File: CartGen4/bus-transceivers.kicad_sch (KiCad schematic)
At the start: 5 parts, among them U4 NXS0108BQX, U6 NXS0108BQX, U7 NXS0108BQX, U8 NXS0104BQX

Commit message: Made general component placement + fixed ADDR
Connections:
- net GB_5V_A0: now also U7.12 (B8); no longer U7.20 (B1)
- net GB_5V_A1: now also U7.13 (B7); no longer U7.18 (B2)
- net GB_5V_A10: now also U6.14 (B6); no longer U6.17 (B3)
- net GB_5V_A11: now also U6.15 (B5); no longer U6.16 (B4)
- net GB_5V_A12: now also U6.16 (B4); no longer U6.15 (B5)
- net GB_5V_A13: now also U6.17 (B3); no longer U6.14 (B6)
- net GB_5V_A14: now also U6.18 (B2); no longer U6.13 (B7)
- net GB_5V_A15: now also U6.20 (B1); no longer U6.12 (B8)
- net GB_5V_A2: now also U7.14 (B6); no longer U7.17 (B3)
- net GB_5V_A3: now also U7.15 (B5); no longer U7.16 (B4)
- net GB_5V_A4: now also U7.16 (B4); no longer U7.15 (B5)
- net GB_5V_A5: now also U7.17 (B3); no longer U7.14 (B6)
- net GB_5V_A6: now also U7.18 (B2); no longer U7.13 (B7)
- net GB_5V_A7: now also U7.20 (B1); no longer U7.12 (B8)
- net GB_5V_A8: now also U6.12 (B8); no longer U6.20 (B1)
- net GB_5V_A9: now also U6.13 (B7); no longer U6.18 (B2)
- net GB_A0: now also U7.9 (A8); no longer U7.1 (A1)
- net GB_A1: now also U7.8 (A7); no longer U7.3 (A2)
- net GB_A10: now also U6.7 (A6); no longer U6.4 (A3)
- net GB_A11: now also U6.6 (A5); no longer U6.5 (A4)
- net GB_A12: now also U6.5 (A4); no longer U6.6 (A5)
- net GB_A13: now also U6.4 (A3); no longer U6.7 (A6)
- net GB_A14: now also U6.3 (A2); no longer U6.8 (A7)
- net GB_A15: now also U6.1 (A1); no longer U6.9 (A8)
- net GB_A2: now also U7.7 (A6); no longer U7.4 (A3)
- net GB_A3: now also U7.6 (A5); no longer U7.5 (A4)
- net GB_A4: now also U7.5 (A4); no longer U7.6 (A5)
- net GB_A5: now also U7.4 (A3); no longer U7.7 (A6)
- net GB_A6: now also U7.3 (A2); no longer U7.8 (A7)
- net GB_A7: now also U7.1 (A1); no longer U7.9 (A8)
- net GB_A8: now also U6.9 (A8); no longer U6.1 (A1)
- net GB_A9: now also U6.8 (A7); no longer U6.3 (A2)
- net GB_CLK: now also U8.5 (A4); no longer U8.2 (A1)
- net GB_CLK_5V: now also U8.10 (B4); no longer U8.13 (B1)
- net GB_CS#: now also U8.2 (A1); no longer U8.4 (A3)
- net GB_CS#_5V: now also U8.13 (B1); no longer U8.11 (B3)
- net GB_RD#: now also U8.3 (A2); no longer U8.5 (A4)
- net GB_RD#_5V: now also U8.12 (B2); no longer U8.10 (B4)
- net GB_WR#: now also U8.4 (A3); no longer U8.3 (A2)
- net GB_WR#_5V: now also U8.11 (B3); no longer U8.12 (B2)

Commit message: Changed most R and C to 0402 size
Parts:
- R14: footprint Resistor_SMD:R_0603_1608Metric_Pad0.98x0.95mm_HandSolder -> Resistor_SMD:R_0402_1005Metric_Pad0.72x0.64mm_HandSolder
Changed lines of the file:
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@@
       (effects (font (size 1.27 1.27)) (justify left))
     )
-    (property "Footprint" "Resistor_SMD:R_0603_1608Metric_Pad0.98x0.95mm_HandSolder" (id 2) (at 47.752 73.66 90)
+    (property "Footprint" "Resistor_SMD:R_0402_1005Metric_Pad0.72x0.64mm_HandSolder" (id 2) (at 47.752 73.66 90)
       (effects (font (size 1.27 1.27)) hide)
     )

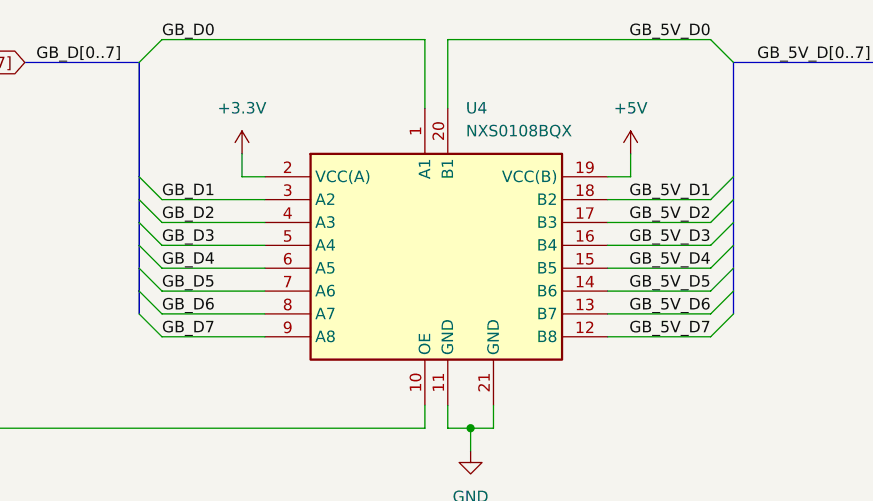
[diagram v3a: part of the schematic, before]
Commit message: Wired power supply
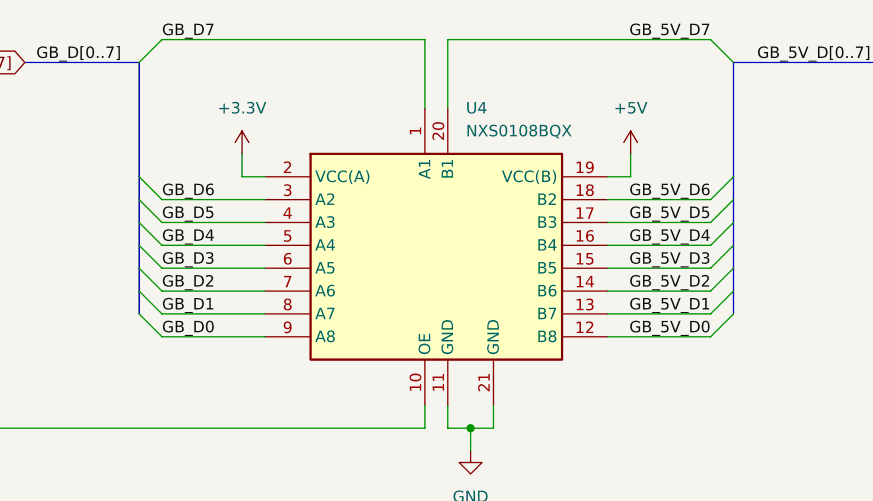
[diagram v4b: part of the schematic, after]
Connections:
- net GB_5V_D0: now also U4.12 (B8); no longer U4.20 (B1)
- net GB_5V_D1: now also U4.13 (B7); no longer U4.18 (B2)
- net GB_5V_D2: now also U4.14 (B6); no longer U4.17 (B3)
- net GB_5V_D3: now also U4.15 (B5); no longer U4.16 (B4)
- net GB_5V_D4: now also U4.16 (B4); no longer U4.15 (B5)
- net GB_5V_D5: now also U4.17 (B3); no longer U4.14 (B6)
- net GB_5V_D6: now also U4.18 (B2); no longer U4.13 (B7)
- net GB_5V_D7: now also U4.20 (B1); no longer U4.12 (B8)
- net GB_D0: now also U4.9 (A8); no longer U4.1 (A1)
- net GB_D1: now also U4.8 (A7); no longer U4.3 (A2)
- net GB_D2: now also U4.7 (A6); no longer U4.4 (A3)
- net GB_D3: now also U4.6 (A5); no longer U4.5 (A4)
- net GB_D4: now also U4.5 (A4); no longer U4.6 (A5)
- net GB_D5: now also U4.4 (A3); no longer U4.7 (A6)
- net GB_D6: now also U4.3 (A2); no longer U4.8 (A7)
- net GB_D7: now also U4.1 (A1); no longer U4.9 (A8)
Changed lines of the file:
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@@
+    (effects (font (size 1.27 1.27)) (justify left bottom))
+  )
+  (label "GB_D4" (at 97.79 46.99 0)
     (effects (font (size 1.27 1.27)) (justify left bottom))
   )
@@
     (effects (font (size 1.27 1.27)) (justify left bottom))
   )
-  (label "GB_D0" (at 97.79 24.13 0)
-    (effects (font (size 1.27 1.27)) (justify left bottom))
+  (label "GB_5V_A[0..7]" (at 176.53 144.78 180)
+    (effects (font (size 1.27 1.27)) (justify right bottom))
   )
-  (label "GB_5V_A[0..7]" (at 176.53 144.78 180)
+  (label "GB_5V_D7" (at 158.75 24.13 180)
+    (effects (font (size 1.27 1.27)) (justify right bottom))
+  )
+  (label "GB_5V_D6" (at 158.75 41.91 180)
     (effects (font (size 1.27 1.27)) (justify right bottom))
   )
@@
     (effects (font (size 1.27 1.27)) (justify right bottom))
   )
-  (label "GB_5V_D5" (at 158.75 52.07 180)
-    (effects (font (size 1.27 1.27)) (justify right bottom))
+  (label "GB_D0" (at 97.79 57.15 0)
+    (effects (font (size 1.27 1.27)) (justify left bottom))
   )
-  (label "GB_5V_D2" (at 158.75 44.45 180)
+  (label "GB_D1" (at 97.79 54.61 0)
+    (effects (font (size 1.27 1.27)) (justify left bottom))
+  )
+  (label "GB_5V_D0" (at 158.75 57.15 180)
     (effects (font (size 1.27 1.27)) (justify right bottom))
   )
@@
   (label "GB_5V_A14" (at 158.75 100.33 180)
     (effects (font (size 1.27 1.27)) (justify right bottom))
-  )
-  (label "GB_D1" (at 97.79 41.91 0)
-    (effects (font (size 1.27 1.27)) (justify left bottom))
   )
   (label "GB_A12" (at 97.79 105.41 0)
@@
     (effects (font (size 1.27 1.27)) (justify left bottom))
   )
-  (label "GB_D7" (at 97.79 57.15 0)
-    (effects (font (size 1.27 1.27)) (justify left bottom))
-  )
-  (label "GB_5V_D3" (at 158.75 46.99 180)
+  (label "GB_5V_D5" (at 158.75 44.45 180)
     (effects (font (size 1.27 1.27)) (justify right bottom))
   )
@@
     (effects (font (size 1.27 1.27)) (justify left bottom))
   )
+  (label "GB_5V_D2" (at 158.75 52.07 180)
+    (effects (font (size 1.27 1.27)) (justify right bottom))
+  )
   (label "GB_5V_A11" (at 158.75 107.95 180)
     (effects (font (size 1.27 1.27)) (justify right bottom))
   )
-  (label "GB_5V_D1" (at 158.75 41.91 180)
+  (label "GB_5V_D1" (at 158.75 54.61 180)
     (effects (font (size 1.27 1.27)) (justify right bottom))
   )
@@
     (effects (font (size 1.27 1.27)) (justify right bottom))
   )
-  (label "GB_D3" (at 97.79 46.99 0)
-    (effects (font (size 1.27 1.27)) (justify left bottom))
-  )
   (label "GB_A1" (at 97.79 172.72 0)
     (effects (font (size 1.27 1.27)) (justify left bottom))
-  )
-  (label "GB_5V_D0" (at 158.75 24.13 180)
-    (effects (font (size 1.27 1.27)) (justify right bottom))
   )
   (label "GB_5V_A10" (at 158.75 110.49 180)
     (effects (font (size 1.27 1.27)) (justify right bottom))
   )
-  (label "GB_5V_D7" (at 158.75 57.15 180)
+  (label "GB_5V_D3" (at 158.75 49.53 180)
     (effects (font (size 1.27 1.27)) (justify right bottom))
   )
@@
     (effects (font (size 1.27 1.27)) (justify left bottom))
   )
-  (label "GB_A3" (at 97.79 167.64 0)
+  (label "GB_5V_D4" (at 158.75 46.99 180)
+    (effects (font (size 1.27 1.27)) (justify right bottom))
+  )
+  (label "GB_D6" (at 97.79 41.91 0)
     (effects (font (size 1.27 1.27)) (justify left bottom))
   )
-  (label "GB_5V_D6" (at 158.75 54.61 180)
-    (effects (font (size 1.27 1.27)) (justify right bottom))
-  )
-  (label "GB_D5" (at 97.79 52.07 0)
+  (label "GB_A3" (at 97.79 167.64 0)
     (effects (font (size 1.27 1.27)) (justify left bottom))
   )
@@
     (effects (font (size 1.27 1.27)) (justify left bottom))
   )
-  (label "GB_D2" (at 97.79 44.45 0)
+  (label "GB_D2" (at 97.79 52.07 0)
     (effects (font (size 1.27 1.27)) (justify left bottom))
   )
   (label "GB_A0" (at 97.79 175.26 0)
+    (effects (font (size 1.27 1.27)) (justify left bottom))
+  )
+  (label "GB_D7" (at 97.79 24.13 0)
     (effects (font (size 1.27 1.27)) (justify left bottom))
   )
@@
     (effects (font (size 1.27 1.27)) (justify left bottom))
   )
+  (label "GB_D5" (at 97.79 44.45 0)
+    (effects (font (size 1.27 1.27)) (justify left bottom))
+  )
   (label "GB_5V_A13" (at 158.75 102.87 180)
     (effects (font (size 1.27 1.27)) (justify right bottom))
-  )
-  (label "GB_D6" (at 97.79 54.61 0)
-    (effects (font (size 1.27 1.27)) (justify left bottom))
   )
   (label "GB_5V_A8" (at 158.75 115.57 180)
@@
     (effects (font (size 1.27 1.27)) (justify right bottom))
   )
+  (label "GB_D3" (at 97.79 49.53 0)
+    (effects (font (size 1.27 1.27)) (justify left bottom))
+  )
   (label "GB_A6" (at 97.79 160.02 0)
     (effects (font (size 1.27 1.27)) (justify left bottom))
@@
     (effects (font (size 1.27 1.27)) (justify left bottom))
   )
-  (label "GB_5V_D4" (at 158.75 49.53 180)
-    (effects (font (size 1.27 1.27)) (justify right bottom))
-  )
-  (label "GB_D4" (at 97.79 49.53 0)
-    (effects (font (size 1.27 1.27)) (justify left bottom))
-  )

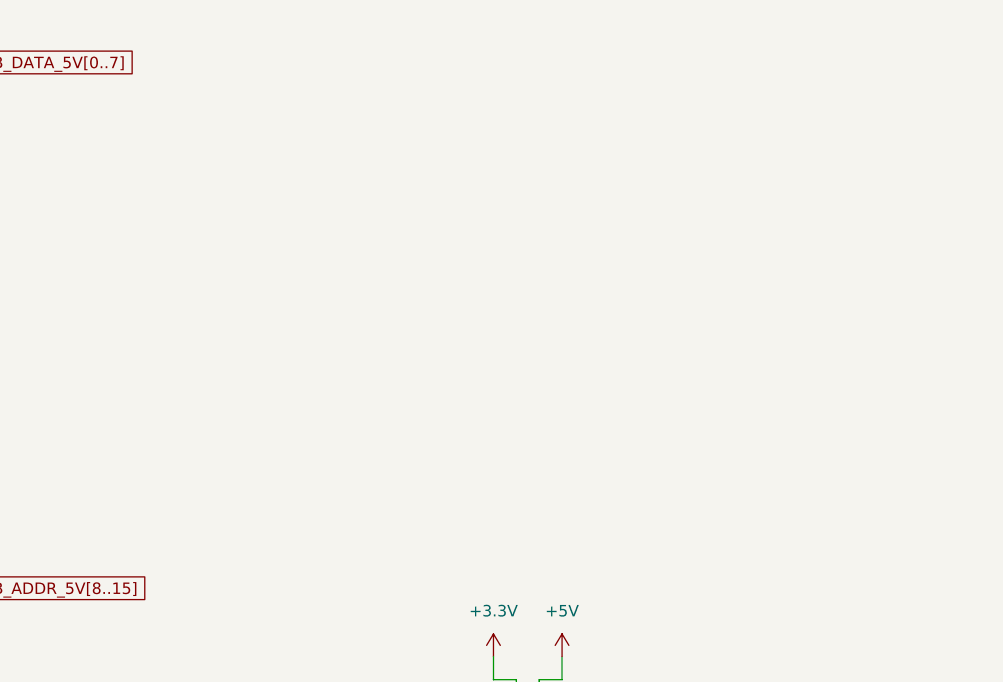
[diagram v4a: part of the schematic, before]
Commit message: Added bypass capacitors to transceivers
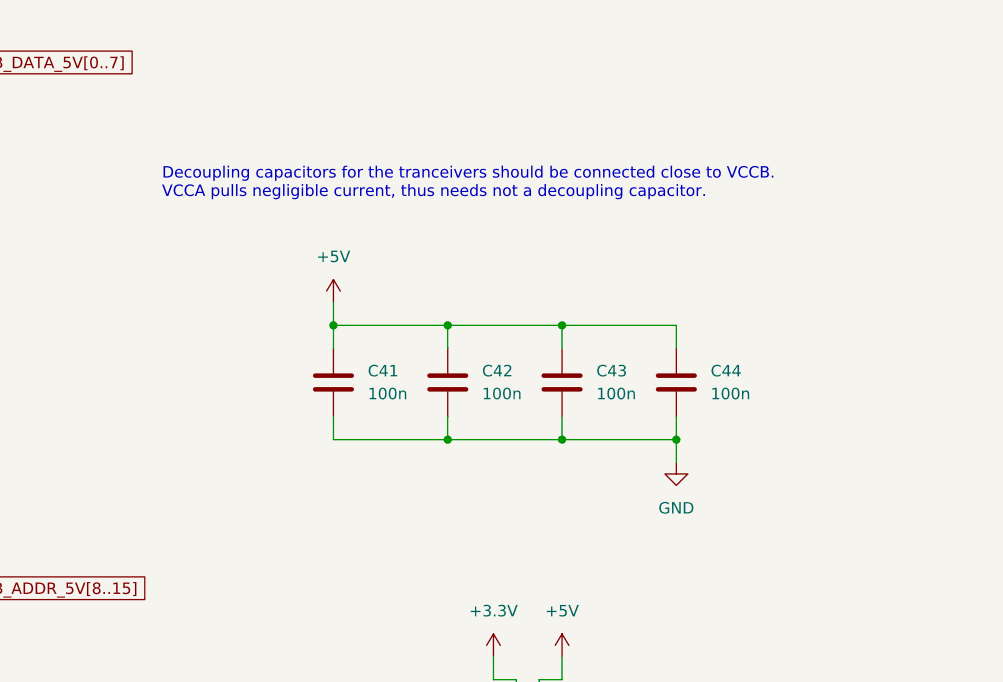
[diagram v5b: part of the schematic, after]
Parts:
- added C41, C42, C43, C44: 100n, Capacitor_SMD:C_0402_1005Metric_Pad0.74x0.62mm_HandSolder, symbol Device:C
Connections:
- net +5V: now also C41.1, C42.1, C43.1, C44.1
- net GND: now also C41.2, C42.2, C43.2, C44.2
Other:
- note added: "Decoupling capacitors for the tranceivers should be connected close to VCCB. VCCA pulls negligible current, thus needs not a decoupling capacitor."

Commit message: Updated field information
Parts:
- C41, C42, C43, C44: Package ID (none) -> 0402
- R14: Notes (none) -> Pulldown resistor for GB_BUS_EN line ensuring cart isolatio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; Package ID (none) -> 0402
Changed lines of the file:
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@@
+      (effects (font (size 1.27 1.27)) hide)
+    )
+    (property "Description" "~" (id 7) (at 231.14 62.23 0)
+      (effects (font (size 1.27 1.27)) hide)
+    )
+    (property "MFN" "~" (id 8) (at 231.14 62.23 0)
+      (effects (font (size 1.27 1.27)) hide)
+    )
+    (property "MFP" "~" (id 9) (at 231.14 62.23 0)
+      (effects (font (size 1.27 1.27)) hide)
+    )
+    (property "Package ID" "0402" (id 10) (at 231.14 62.23 0)
       (effects (font (size 1.27 1.27)) hide)
     )
@@
     )
     (property "Source" "ANY" (id 6) (at 218.44 62.23 0)
+      (effects (font (size 1.27 1.27)) hide)
+    )
+    (property "Description" "~" (id 7) (at 218.44 62.23 0)
+      (effects (font (size 1.27 1.27)) hide)
+    )
+    (property "MFN" "~" (id 8) (at 218.44 62.23 0)
+      (effects (font (size 1.27 1.27)) hide)
+    )
+    (property "MFP" "~" (id 9) (at 218.44 62.23 0)
+      (effects (font (size 1.27 1.27)) hide)
+    )
+    (property "Package ID" "0402" (id 10) (at 218.44 62.23 0)
       (effects (font (size 1.27 1.27)) hide)
     )
@@
       (effects (font (size 1.27 1.27)) hide)
     )
+    (property "Description" "~" (id 7) (at 243.84 62.23 0)
+      (effects (font (size 1.27 1.27)) hide)
+    )
+    (property "MFN" "~" (id 8) (at 243.84 62.23 0)
+      (effects (font (size 1.27 1.27)) hide)
+    )
+    (property "MFP" "~" (id 9) (at 243.84 62.23 0)
+      (effects (font (size 1.27 1.27)) hide)
+    )
+    (property "Package ID" "0402" (id 10) (at 243.84 62.23 0)
+      (effects (font (size 1.27 1.27)) hide)
+    )
     (pin "1")
     (pin "2")
@@
     )
     (property "Critical" "Y" (id 6) (at 49.53 73.66 0)
+      (effects (font (size 1.27 1.27)) hide)
+    )
+    (property "Notes" "Pulldown resistor for GB_BUS_EN line ensuring cart isolation during startup" (id 7) (at 49.53 73.66 0)
+      (effects (font (size 1.27 1.27)) hide)
+    )
+    (property "Description" "~" (id 8) (at 49.53 73.66 0)
+      (effects (font (size 1.27 1.27)) hide)
+    )
+    (property "MFN" "~" (id 9) (at 49.53 73.66 0)
+      (effects (font (size 1.27 1.27)) hide)
+    )
+    (property "MFP" "~" (id 10) (at 49.53 73.66 0)
+      (effects (font (size 1.27 1.27)) hide)
+    )
+    (property "Package ID" "0402" (id 11) (at 49.53 73.66 0)
       (effects (font (size 1.27 1.27)) hide)
     )
@@
       (effects (font (size 1.27 1.27)) hide)
     )
+    (property "Description" "~" (id 7) (at 256.54 62.23 0)
+      (effects (font (size 1.27 1.27)) hide)
+    )
+    (property "MFN" "~" (id 8) (at 256.54 62.23 0)
+      (effects (font (size 1.27 1.27)) hide)
+    )
+    (property "MFP" "~" (id 9) (at 256.54 62.23 0)
+      (effects (font (size 1.27 1.27)) hide)
+    )
+    (property "Package ID" "0402" (id 10) (at 256.54 62.23 0)
+      (effects (font (size 1.27 1.27)) hide)
+    )

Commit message: Updated some component fields
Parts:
- C41, C42, C43, C44: Supplier suggestion (none) -> https://nl.mouser.com/ProductDetail/Murata-Electronics/GRM1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; Tolerance (none) -> 20%; Voltage (none) -> 3V3
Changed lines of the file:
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@@
+      (effects (font (size 1.27 1.27)) hide)
+    )
+    (property "Supplier suggestion" "https://nl.mouser.com/ProductDetail/Murata-Electronics/GRM155R61C104KA88J?qs=sGAEpiMZZMsh%252B1woXyUXj8YF%2FGivH5Kx4uStnYyl8jU%3D" (id 11) (at 231.14 62.23 0)
+      (effects (font (size 1.27 1.27)) hide)
+    )
+    (property "Tolerance" "20%" (id 12) (at 231.14 62.23 0)
+      (effects (font (size 1.27 1.27)) hide)
+    )
+    (property "Voltage" "3V3" (id 13) (at 231.14 62.23 0)
       (effects (font (size 1.27 1.27)) hide)
     )
@@
     )
     (property "Package ID" "0402" (id 10) (at 218.44 62.23 0)
+      (effects (font (size 1.27 1.27)) hide)
+    )
+    (property "Supplier suggestion" "https://nl.mouser.com/ProductDetail/Murata-Electronics/GRM155R61C104KA88J?qs=sGAEpiMZZMsh%252B1woXyUXj8YF%2FGivH5Kx4uStnYyl8jU%3D" (id 11) (at 218.44 62.23 0)
+      (effects (font (size 1.27 1.27)) hide)
+    )
+    (property "Tolerance" "20%" (id 12) (at 218.44 62.23 0)
+      (effects (font (size 1.27 1.27)) hide)
+    )
+    (property "Voltage" "3V3" (id 13) (at 218.44 62.23 0)
       (effects (font (size 1.27 1.27)) hide)
     )
@@
       (effects (font (size 1.27 1.27)) hide)
     )
+    (property "Supplier suggestion" "https://nl.mouser.com/ProductDetail/Murata-Electronics/GRM155R61C104KA88J?qs=sGAEpiMZZMsh%252B1woXyUXj8YF%2FGivH5Kx4uStnYyl8jU%3D" (id 11) (at 243.84 62.23 0)
+      (effects (font (size 1.27 1.27)) hide)
+    )
+    (property "Tolerance" "20%" (id 12) (at 243.84 62.23 0)
+      (effects (font (size 1.27 1.27)) hide)
+    )
+    (property "Voltage" "3V3" (id 13) (at 243.84 62.23 0)
+      (effects (font (size 1.27 1.27)) hide)
+    )
     (pin "1")
     (pin "2")
@@
       (effects (font (size 1.27 1.27)) hide)
     )
+    (property "Supplier suggestion" "https://nl.mouser.com/ProductDetail/Murata-Electronics/GRM155R61C104KA88J?qs=sGAEpiMZZMsh%252B1woXyUXj8YF%2FGivH5Kx4uStnYyl8jU%3D" (id 11) (at 256.54 62.23 0)
+      (effects (font (size 1.27 1.27)) hide)
+    )
+    (property "Tolerance" "20%" (id 12) (at 256.54 62.23 0)
+      (effects (font (size 1.27 1.27)) hide)
+    )
+    (property "Voltage" "3V3" (id 13) (at 256.54 62.23 0)
+      (effects (font (size 1.27 1.27)) hide)
+    )
